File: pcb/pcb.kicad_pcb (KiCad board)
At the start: 2 copper layers, 347.9 x 133.5 mm, 248 parts, among them J1 USB_C_Receptacle_USB2.0_16P, SW1 SW_Push, U1 USBLC6-2SC6, U2 ATmega32U4-A, Y1 16MHz

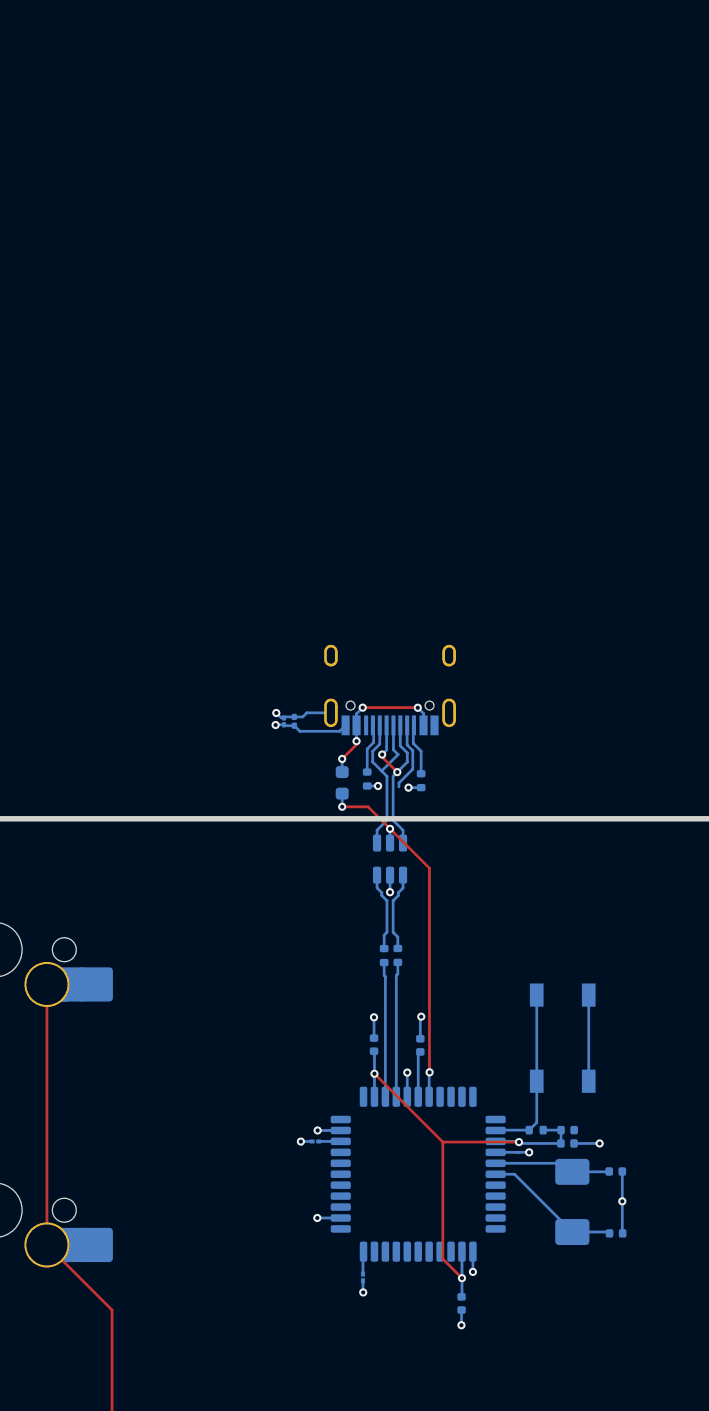
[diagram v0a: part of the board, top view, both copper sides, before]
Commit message: change MCU to STM32F0
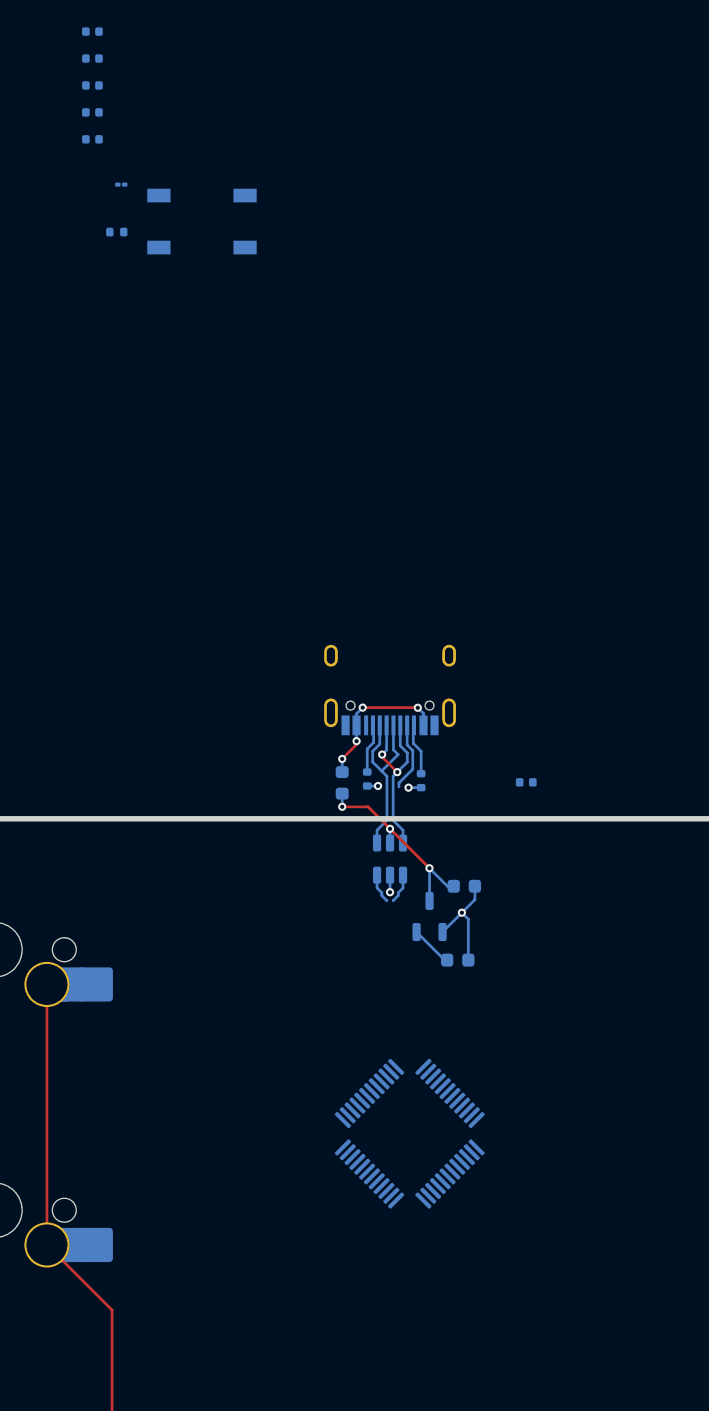
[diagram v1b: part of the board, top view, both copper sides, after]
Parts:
- removed R4: 1M, Resistor_SMD:R_0201_0603Metric
- removed R5, R6: 22, Resistor_SMD:R_0402_1005Metric
- removed R7: 10k, Resistor_SMD:R_01005_0402Metric
- removed Y1: 16MHz, Crystal:Crystal_SMD_0603-2Pin_6.0x3.5mm
- added U3: STM32F072CBTx, Package_QFP:LQFP-48_7x7mm_P0.5mm, B.Cu at (335.1, 51.6)
- C1: value 10u -> 100n
- C5: value 1n -> 100n; footprint Capacitor_SMD:C_01005_0402Metric -> Capacitor_SMD:C_0402_1005Metric
- C6: value ~22p -> 10u
- C7: value ~22p -> 100n; footprint Capacitor_SMD:C_0402_1005Metric -> Capacitor_SMD:C_01005_0402Metric
- C8: value 100n -> 1u; footprint Capacitor_SMD:C_01005_0402Metric -> Capacitor_SMD:C_0603_1608Metric
- C9: footprint Capacitor_SMD:C_0402_1005Metric -> Capacitor_SMD:C_0603_1608Metric
- U2: value ATmega32U4-A -> XC6206PxxxMR; footprint Package_QFP:TQFP-44_10x10mm_P0.8mm -> Package_TO_SOT_SMD:SOT-23-3
- moved C4 91.2 mm to (311.9, -23.1), turned to 180 degrees
- moved C6 88.7 mm to (311.9, -21.2)
- moved C1 87.5 mm to (311.9, -29.0)
- moved C3 84.8 mm to (311.9, -25.1)
- moved C7 80.7 mm to (314.0, -17.9), turned to 180 degrees
- moved C2 75.0 mm to (311.9, -27.1), turned to 180 degrees
- moved R3 72.5 mm to (313.7, -14.4)
- moved SW1 65.3 mm to (319.9, -15.2), turned to 180 degrees
- moved C8 21.6 mm to (339.1, 33.5)
- moved U2 18.9 mm to (336.6, 35.7), turned to 90 degrees
- moved C5 18.3 mm to (343.7, 25.9), turned to 180 degrees
- moved C9 6.81 mm to (338.6, 38.9), turned to 0 degrees
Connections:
- C1 pad 1: GND -> +3.3V
- C1 pad 2: VBUS -> GND
- C2 pad 1: GND -> +3.3V
- C2 pad 2: VBUS -> GND
- C3 pad 1: GND -> +3.3V
- C3 pad 2: VBUS -> GND
- C4 pad 1: GND -> +3.3V
- C4 pad 2: VBUS -> GND
- C5 pad 1: EARTH -> +3.3V
- C6 pad 1: GND -> +3.3V
- C6 pad 2: Net-(U2-XTAL1) -> GND
- C7 pad 1: Net-(U2-XTAL2) -> GND
- C7 pad 2: GND -> Net-(U3-NRST)
- C8 pad 1: GND -> VBUS
- C8 pad 2: Net-(U2-AREF) -> GND
- C9 pad 1: Net-(U2-UCAP) -> +3.3V
- J1 pad S1: EARTH -> GND
- R3 pad 1: VBUS -> BOOT0
- R3 pad 2: Net-(U2-~{RESET}) -> GND
- SW1 pad 1: GND -> +3.3V
- SW1 pad 2: Net-(U2-~{RESET}) -> BOOT0
- U2 pad 1: Ro5 -> GND
- U2 pad 2: VBUS -> +3.3V
- U2 pad 3: Net-(U2-D-) -> VBUS
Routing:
- net VBUS: track 64.0 -> 15.0 mm, vias 6 -> 3
- net GND: track 36.2 -> 11.0 mm, vias 16 -> 4
- net Net-(U2-~{RESET}): track 12.6 -> 0.00 mm
- net Net-(U2-XTAL1): track 10.1 -> 0.00 mm
- net Net-(U2-D+): track 9.87 -> 0.00 mm
- net Net-(U2-D-): track 9.85 -> 0.00 mm
- net Net-(U2-XTAL2): track 8.57 -> 0.00 mm
- net EARTH: track 4.20 -> 0.00 mm, vias 1 -> 0
- net D+: track 5.82 -> 2.16 mm
- net D-: track 5.77 -> 2.16 mm
- net Net-(U2-UCAP): track 3.35 -> 0.00 mm
- net +3.3V: track 0.00 -> 3.09 mm
- net Net-(U2-~{HWB}/PE2): track 1.65 -> 0.00 mm
- net Net-(U2-AREF): track 1.60 -> 0.00 mm

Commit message: ESD protection
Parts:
- U1: footprint PCM_marbastlib-various:SOT-23-6-routable -> Package_TO_SOT_SMD:SOT-23-6
- moved C9 13.9 mm to (342.4, 52.2)
- moved J1 13.9 mm to (337.5, 31.0)
- moved R2 13.9 mm to (339.8, 39.1)
- moved C8 13.9 mm to (342.9, 46.8)
- moved F1 13.9 mm to (334.0, 39.2)
- moved U2 13.9 mm to (340.4, 49.0)
- moved C5 13.9 mm to (347.4, 39.2)
- moved R1 13.9 mm to (335.8, 39.0)
- moved U1 12.7 mm to (337.5, 43.6)
- moved U3 3.71 mm to (332.7, 54.4), turned to 45 degrees
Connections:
- net /USB1.D+ renamed /usb+
- net /USB1.D- renamed /usb-
- U1 pad 2: VBUS -> GND
- U1 pad 5: GND -> VBUS
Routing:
- net VBUS: track 15.0 -> 7.21 mm
- net GND: track 11.0 -> 17.9 mm, vias 4 -> 2
- net D+: track 2.16 -> 8.38 mm
- net D-: track 2.16 -> 8.00 mm
- net unconnected-(J1-SBU1-PadA8): track 5.10 -> 0.00 mm
- net Net-(J1-CC2): track 3.79 -> 0.07 mm
- net Net-(J1-CC1): track 3.63 -> 0.07 mm
- net /usb-: track 13.5 -> 11.4 mm
- net /usb+: track 13.6 -> 11.6 mm

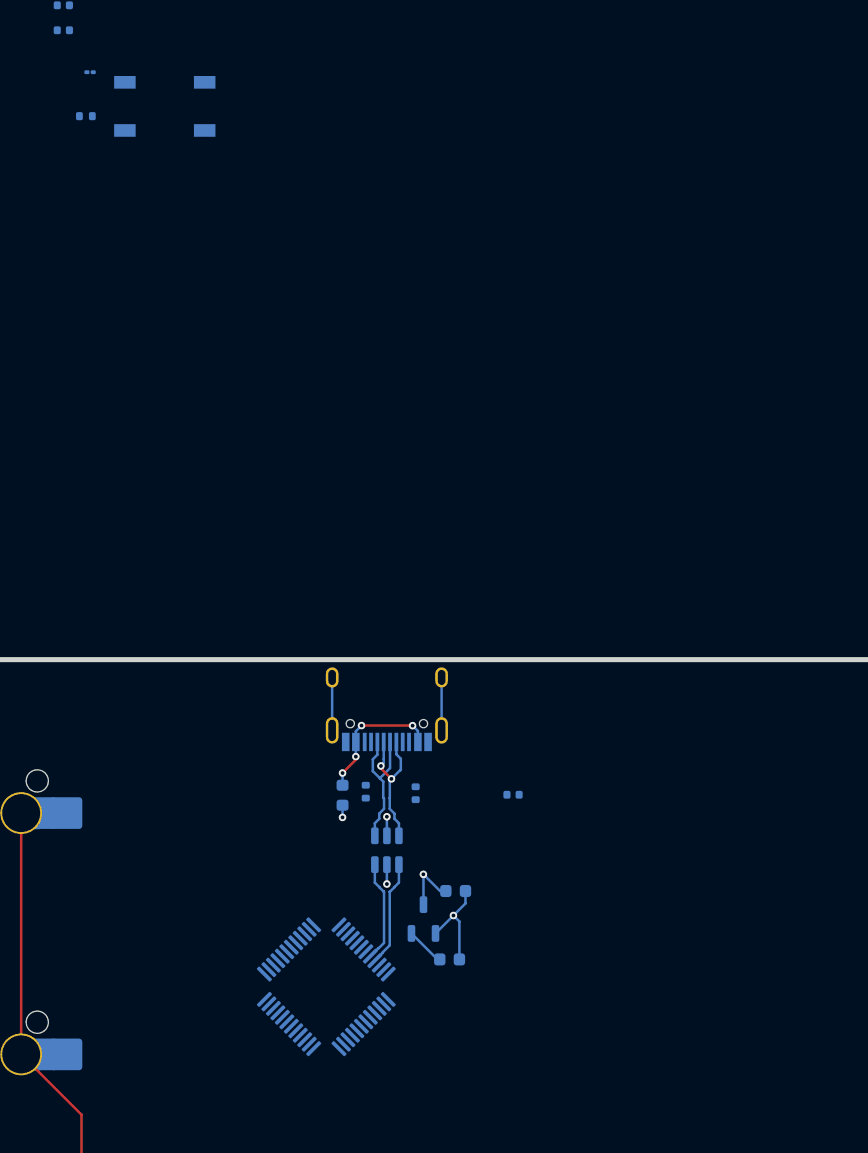
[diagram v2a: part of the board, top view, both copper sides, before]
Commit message: Connecting MCU
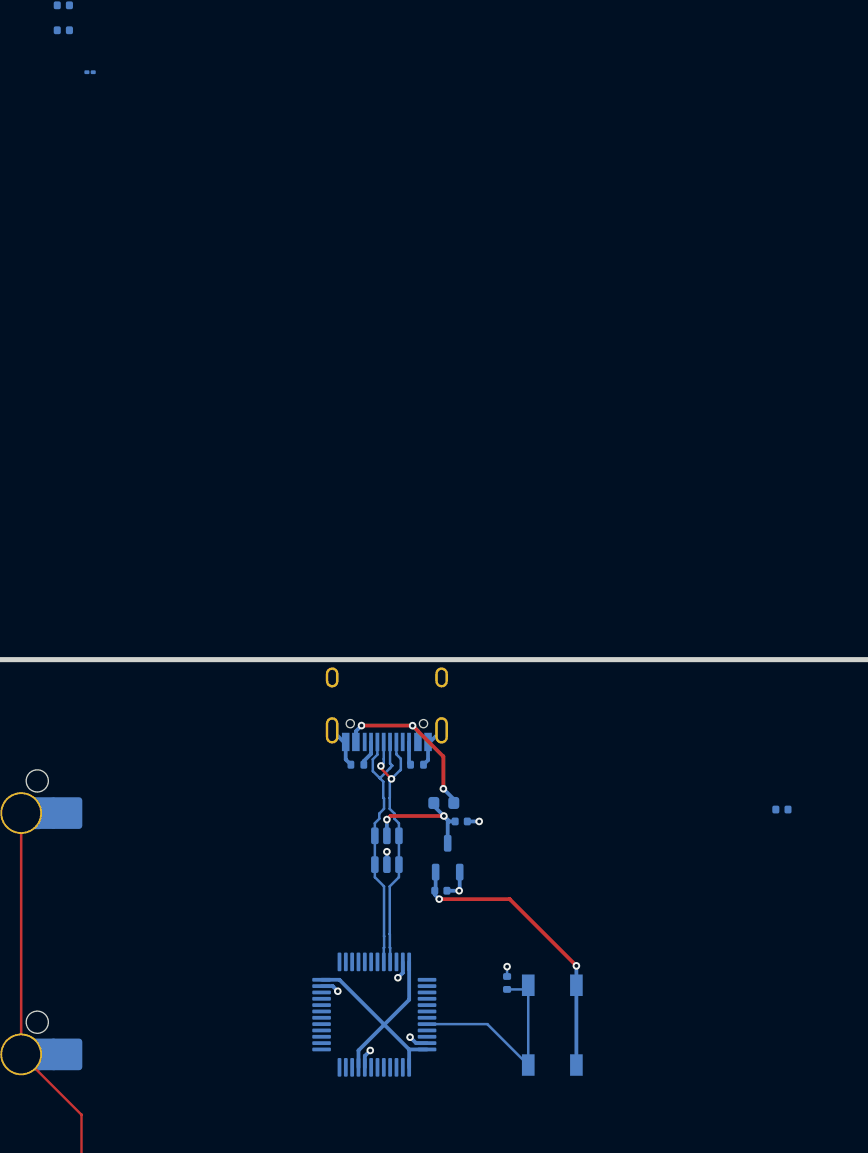
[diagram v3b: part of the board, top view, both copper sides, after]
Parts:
- C8, C9: footprint Capacitor_SMD:C_0603_1608Metric -> Capacitor_SMD:C_0402_1005Metric
- F1: value 500mA -> 500m
- moved SW1 78.7 mm to (350.5, 57.4), turned to 90 degrees
- moved R3 76.1 mm to (347.0, 54.0), turned to 90 degrees
- moved C5 21.3 mm to (368.7, 40.4)
- moved F1 8.02 mm to (342.0, 39.8), turned to 180 degrees
- moved C8 5.51 mm to (343.4, 41.3)
- moved C9 5.47 mm to (341.7, 46.8)
- moved U2 5.21 mm to (342.3, 44.2)
- moved U3 4.38 mm to (336.5, 56.5), turned to 90 degrees
- moved R2 2.25 mm to (339.9, 36.8), turned to 0 degrees
- moved R1 2.23 mm to (335.1, 36.8), turned to 180 degrees
- turned U1 to 90 degrees
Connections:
- J1 pad A6: /usb+ -> D+
- J1 pad A7: /usb- -> D-
- J1 pad B6: /usb+ -> D+
- J1 pad B7: /usb- -> D-
- U1 pad 1: /usb- -> D+
- U1 pad 3: /usb+ -> D-
- U1 pad 4: D+ -> D-
- U1 pad 6: D- -> D+
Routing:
- net +3.3V: track 3.09 -> 45.1 mm, vias 0 -> 2
- net BOOT0: track 0.00 -> 17.4 mm
- net D-: track 8.00 -> 21.4 mm
- net D+: track 8.38 -> 21.5 mm, vias 0 -> 2
- net /usb+: track 11.6 -> 0.00 mm, vias 2 -> 0
- net /usb-: track 11.4 -> 0.00 mm
- net Net-(F1-Pad1): track 10.8 -> 14.4 mm, vias 4 -> 3
- net VBUS: track 7.21 -> 10.6 mm, vias 3 -> 2
- net Net-(J1-CC1): track 0.07 -> 2.10 mm
- net Net-(J1-CC2): track 0.07 -> 1.91 mm
- net GND: vias 2 -> 8

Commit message: Connects all components on the PCB
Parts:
- added REF**: MountingHole_2mm, MountingHole:MountingHole_2mm, F.Cu at (31.2, 31.2)
- added REF**: MountingHole_2mm, MountingHole:MountingHole_2mm, F.Cu at (31.0, 159.6)
- added REF**: MountingHole_2mm, MountingHole:MountingHole_2mm, F.Cu at (373.9, 159.5)
- added REF**: MountingHole_2mm, MountingHole:MountingHole_2mm, F.Cu at (373.5, 31.5)
- C7: footprint Capacitor_SMD:C_01005_0402Metric -> Capacitor_SMD:C_0201_0603Metric
- SW1: footprint Button_Switch_SMD:SW_SPST_TL3342 -> PCM_marbastlib-various:SW_SPST_SKQG_WithStem
- U1: footprint Package_TO_SOT_SMD:SOT-23-6 -> PCM_marbastlib-various:SOT-23-6-routable
- moved C1 95.0 mm to (338.2, 62.3), turned to 0 degrees
- moved C3 90.5 mm to (338.8, 61.3), turned to 0 degrees
- moved C4 89.4 mm to (333.1, 63.8), turned to -90 degrees
- moved C7 83.8 mm to (334.1, 63.6), turned to 90 degrees
- moved C2 82.5 mm to (329.7, 53.5), turned to 90 degrees
- moved C6 79.3 mm to (338.8, 53.4), turned to -90 degrees
- moved C5 33.4 mm to (337.7, 52.9), turned to 90 degrees
- moved SW1 5.53 mm to (345.8, 54.5)
- moved R3 5.53 mm to (342.3, 51.1)
- moved C8 2.67 mm to (340.9, 42.4)
- moved U1 2.67 mm to (335.0, 44.6)
- moved J1 2.67 mm to (335.0, 32.0)
- moved F1 2.67 mm to (339.5, 40.9)
- moved C9 2.67 mm to (339.3, 47.8)
- moved R1 2.67 mm to (332.7, 37.9)
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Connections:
- U3 pad 16: unconnected-(U3-PA6-Pad16) -> Ro6
- U3 pad 17: unconnected-(U3-PA7-Pad17) -> Co0
- U3 pad 29: unconnected-(U3-PA8-Pad29) -> Co1
- U3 pad 30: unconnected-(U3-PA9-Pad30) -> Co2
- U3 pad 31: unconnected-(U3-PA10-Pad31) -> Co3
- U3 pad 39: Ro6 -> unconnected-(U3-PB3-Pad39)
- U3 pad 40: Co0 -> unconnected-(U3-PB4-Pad40)
- U3 pad 41: Co1 -> unconnected-(U3-PB5-Pad41)
- U3 pad 42: Co2 -> unconnected-(U3-PB6-Pad42)
- U3 pad 43: Co3 -> unconnected-(U3-PB7-Pad43)
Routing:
- net GND: track 17.9 -> 25.9 mm, vias 8 -> 15
- net +3.3V: track 45.1 -> 52.8 mm, vias 2 -> 3
- net BOOT0: track 17.4 -> 14.2 mm
- net Net-(U3-NRST): track 0.00 -> 1.59 mm

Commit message: Mouting holes
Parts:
- added REF**: MountingHole_2mm, MountingHole:MountingHole_2mm, F.Cu at (202.5, 142.9)
- added REF**: MountingHole_2mm, MountingHole:MountingHole_2mm, F.Cu at (202.5, 47.6)
- moved REF** 0.65 mm to (373.9, 31.0)
- moved REF** 0.26 mm to (31.0, 31.0)
- moved REF** 0.15 mm to (366.7, 142.9)
- moved REF** 0.14 mm to (366.7, 104.8)
- moved REF** 0.07 mm to (31.1, 159.5)
- moved REF** 0.05 mm to (373.9, 159.5)
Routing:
- net Co13: track 116.3 -> 117.0 mm
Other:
- board size 347.9 x 133.5 mm -> 347.8 x 133.5 mm

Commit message: 200 more connections to go
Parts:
- moved D105 9.36 mm to (223.7, 150.0)
- moved D106 9.36 mm to (247.5, 150.0)
- moved D107 9.36 mm to (268.9, 150.0)
- moved D109 9.36 mm to (307.0, 150.0)
- moved D110 9.36 mm to (326.1, 150.0)
- moved D111 9.36 mm to (345.1, 150.0)
- moved D108 9.36 mm to (288.0, 150.0)
- moved D82 9.33 mm to (37.9, 131.0)
- moved D83 9.33 mm to (59.4, 131.0)
- moved D84 9.33 mm to (78.4, 131.0)
- moved D85 9.33 mm to (97.5, 131.0)
- moved D86 9.33 mm to (116.5, 131.0)
- moved D87 9.33 mm to (135.6, 131.0)
- moved D88 9.33 mm to (154.6, 131.0)
- moved D90 9.33 mm to (192.7, 131.0)
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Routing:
- net Ro5: track 0.00 -> 288.1 mm
- net Ro6: track 162.0 -> 307.2 mm
- net Net-(D111-A): track 0.00 -> 6.99 mm
- net Net-(D110-A): track 0.00 -> 6.99 mm
- net Net-(D109-A): track 0.00 -> 6.99 mm
- net Net-(D108-A): track 0.00 -> 6.99 mm
- net Net-(D107-A): track 0.00 -> 6.99 mm
- net Net-(D106-A): track 0.00 -> 6.99 mm
- net Net-(D105-A): track 0.00 -> 6.99 mm
- net Net-(D97-A): track 0.00 -> 6.94 mm
- net Net-(D96-A): track 0.00 -> 6.94 mm
- net Net-(D95-A): track 0.00 -> 6.94 mm
- net Net-(D94-A): track 0.00 -> 6.94 mm
- net Net-(D93-A): track 0.00 -> 6.94 mm
- net Net-(D92-A): track 0.00 -> 6.94 mm
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
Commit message: 100 more connections to go
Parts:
- moved D65 9.58 mm to (364.2, 102.0)
- moved D98 9.33 mm to (345.1, 131.0)
- moved D66 9.30 mm to (37.9, 112.0)
- moved D67 9.30 mm to (59.4, 112.0)
- moved D68 9.30 mm to (78.4, 112.0)
- moved D69 9.30 mm to (97.5, 112.0)
- moved D70 9.30 mm to (116.5, 112.0)
- moved D71 9.30 mm to (135.6, 112.0)
- moved D72 9.30 mm to (154.6, 112.0)
- moved D74 9.30 mm to (192.7, 112.0)
- moved D75 9.30 mm to (211.8, 112.0)
- moved D76 9.30 mm to (230.8, 112.0)
- moved D77 9.30 mm to (249.9, 112.0)
- moved D78 9.30 mm to (278.4, 112.0)
- moved D79 9.30 mm to (307.0, 112.0)
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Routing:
- net Ro3: track 0.00 -> 330.0 mm
- net Ro4: track 0.00 -> 307.2 mm
- net Ro2: track 0.00 -> 271.5 mm
- net Ro5: track 288.1 -> 330.4 mm
- net Net-(D65-A): track 0.00 -> 7.37 mm
- net Net-(D98-A): track 0.00 -> 6.94 mm
- net Net-(D81-A): track 0.00 -> 6.89 mm
- net Net-(D80-A): track 0.00 -> 6.89 mm
- net Net-(D79-A): track 0.00 -> 6.89 mm
- net Net-(D78-A): track 0.00 -> 6.89 mm
- net Net-(D77-A): track 0.00 -> 6.89 mm
- net Net-(D76-A): track 0.00 -> 6.89 mm
- net Net-(D75-A): track 0.00 -> 6.89 mm
- net Net-(D74-A): track 0.00 -> 6.89 mm
- net Net-(D73-A): track 0.00 -> 6.89 mm
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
